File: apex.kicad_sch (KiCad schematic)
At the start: 15 parts, among them J1 USB_C_Receptacle_USB2.0_16P, U1 AP7363-33D-13, U2 USBLC6-2P6

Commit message: re-added symbols
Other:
- note added: "5v-to-3.3v"
- note added: "GND-to-SHIELD"
- note added: "ON LIGHT"
- note added: "USB Configuration Channel"
- note added: "USB ESD Protection"
- note added: "USB-C Connector"
- moved on the sheet: C1, C2, C3, H1, H2, H3, H4, J1, LED1, R1, R2, R3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

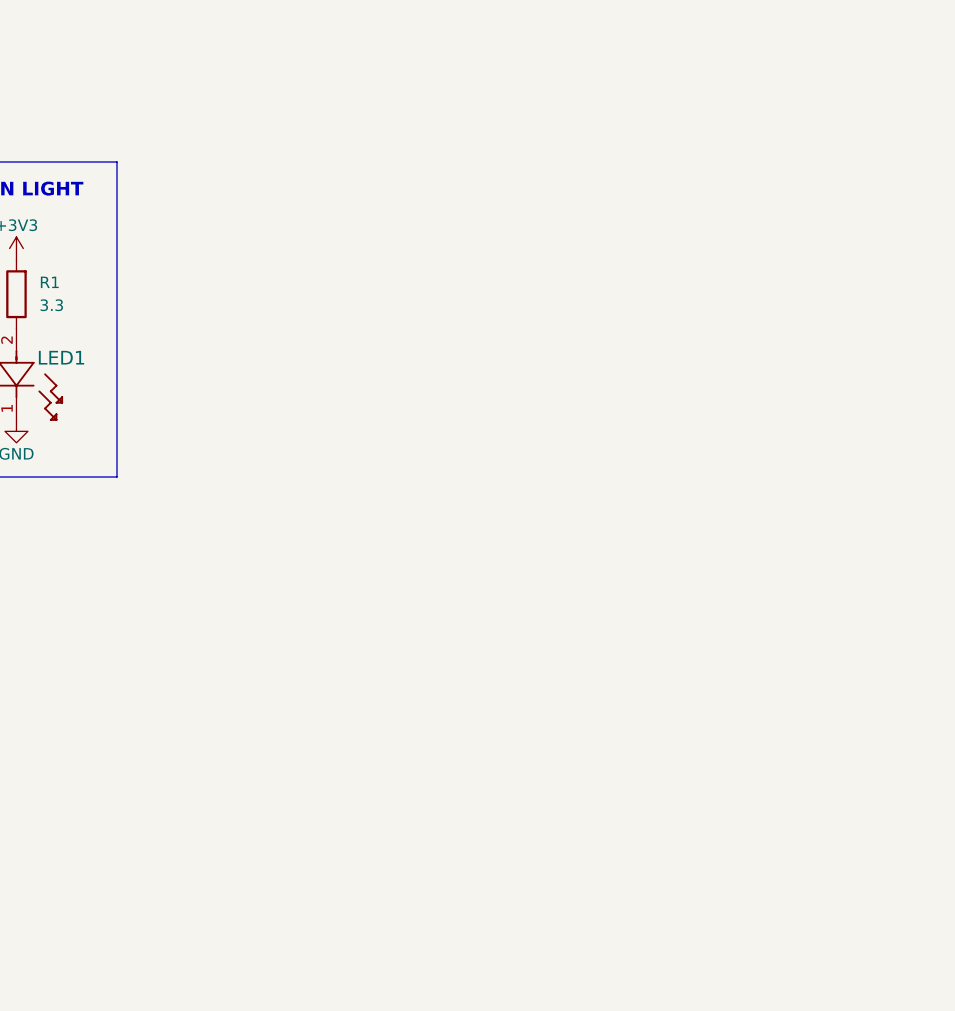
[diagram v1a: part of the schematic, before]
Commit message: started footprint
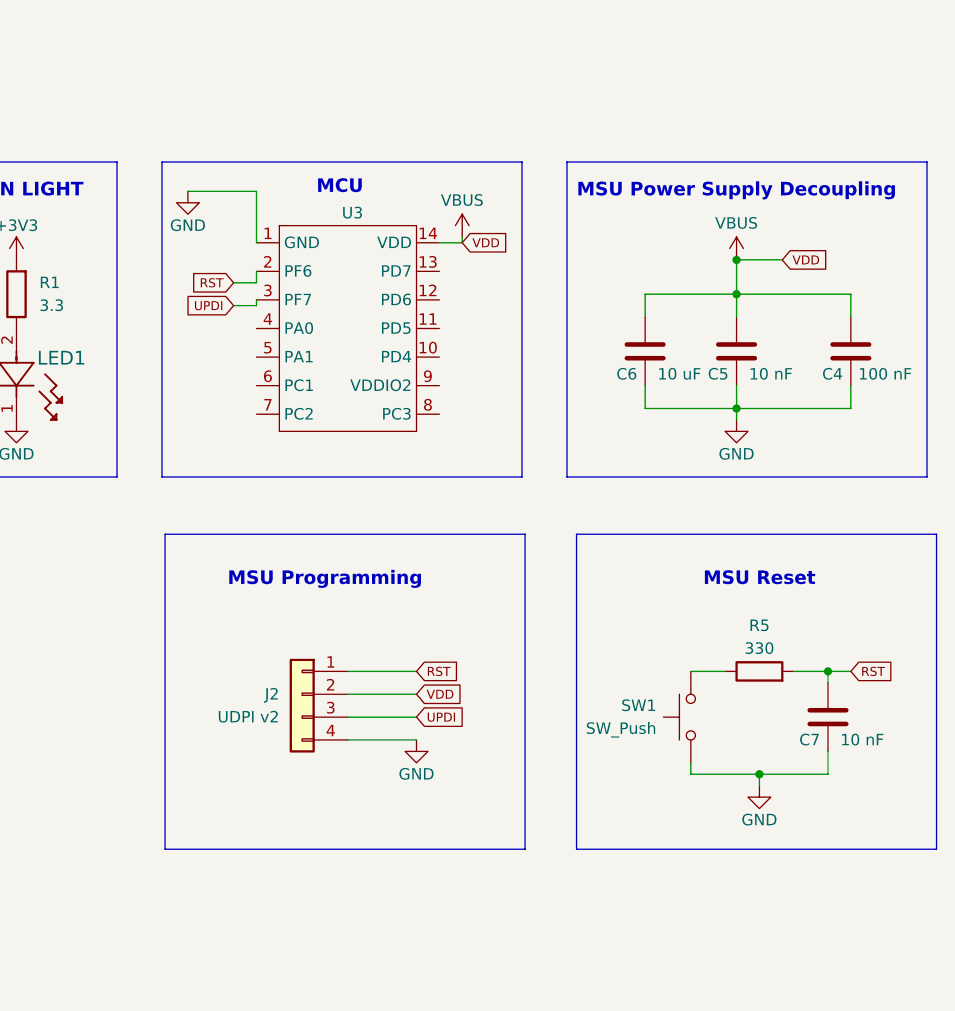
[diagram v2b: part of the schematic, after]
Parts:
- added C4: 100 nF, Capacitor_SMD:C_0805_2012Metric, symbol Device:C
- added C5, C7: 10 nF, Capacitor_SMD:C_0805_2012Metric, symbol Device:C
- added C6: 10 uF, Capacitor_SMD:C_0805_2012Metric, symbol Device:C
- added J2: UDPI v2, symbol Connector_Generic:Conn_01x04
- added R5: 330, Resistor_SMD:R_0805_2012Metric, symbol Device:R
- added SW1: SW_Push, symbol Switch:SW_Push
- added U3: ~, symbol avr66dd14:AVR66DD14
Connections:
- net GND: now also C4.1, C5.1, C6.1, C7.1, J2.4 (Pin_4), SW1.2, U3.1 (GND)
- net VBUS: now also C4.2, C5.2, C6.2, J2.2 (Pin_2), U3.14 (VDD)
- new net: R5.1, SW1.1
- new net RST: C7.2, J2.1 (Pin_1), R5.2, U3.2 (PF6)
- new net UPDI: J2.3 (Pin_3), U3.3 (PF7)
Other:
- note added: "MCU"
- note added: "MSU Power Supply Decoupling"
- note added: "MSU Programming"
- note added: "MSU Reset"

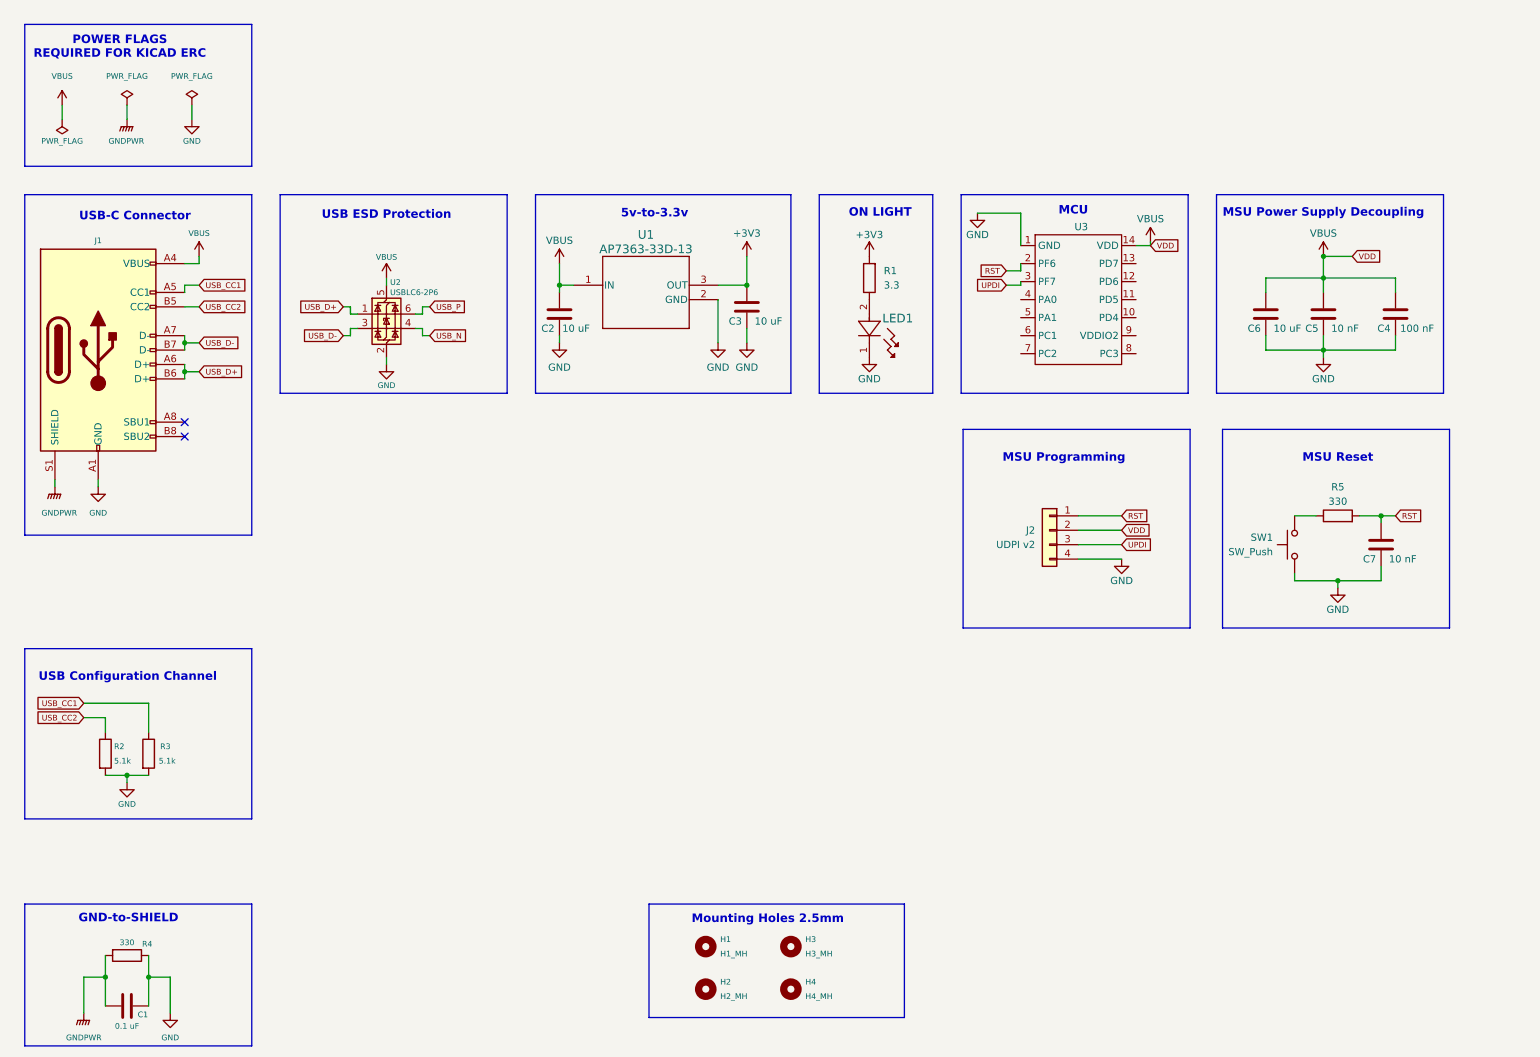
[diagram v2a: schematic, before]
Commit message: added split worksheets
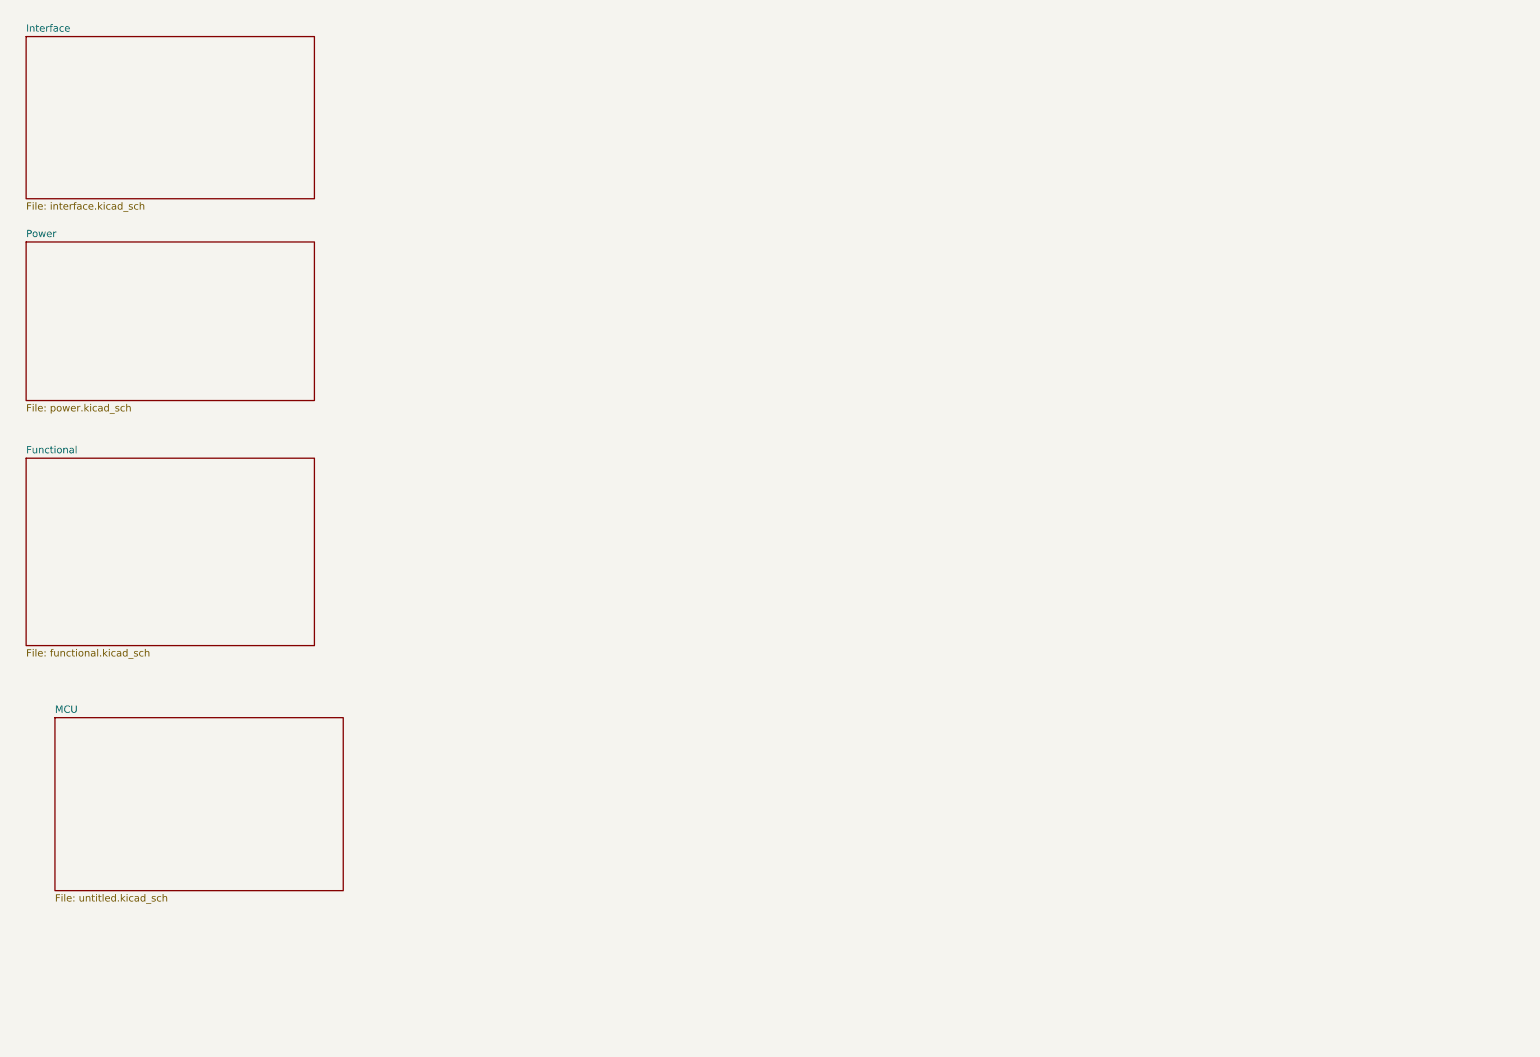
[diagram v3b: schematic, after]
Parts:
- removed C1: 0.1 uF, Capacitor_SMD:C_0805_2012Metric, symbol Device:C
- removed C2, C3, C6: 10 uF, Capacitor_SMD:C_0805_2012Metric, symbol Device:C
- removed C4: 100 nF, Capacitor_SMD:C_0805_2012Metric, symbol Device:C
- removed C5, C7: 10 nF, Capacitor_SMD:C_0805_2012Metric, symbol Device:C
- removed H1: H1_MH, MountingHole:MountingHole_2.5mm_Pad, symbol Mechanical:MountingHole
- removed H2: H2_MH, MountingHole:MountingHole_2.5mm_Pad, symbol Mechanical:MountingHole
- removed H3: H3_MH, MountingHole:MountingHole_2.5mm_Pad, symbol Mechanical:MountingHole
- removed H4: H4_MH, MountingHole:MountingHole_2.5mm_Pad, symbol Mechanical:MountingHole
- removed J1: USB_C_Receptacle_USB2.0_16P, Connector_USB:USB_C_Receptacle_GCT_USB4110, symbol Connector:USB_C_Receptacle_USB2.0_16P
- removed J2: UDPI v2, symbol Connector_Generic:Conn_01x04
- removed LED1: 150080BS75000, LEDBS75000_WRE:LED_BS75000_WRE, symbol 150080BS75000:150080BS75000
- removed R1: 3.3, Resistor_SMD:R_0805_2012Metric, symbol Device:R
- removed R2, R3: 5.1k, Resistor_SMD:R_0805_2012Metric, symbol Device:R
- removed R4, R5: 330, Resistor_SMD:R_0805_2012Metric, symbol Device:R
- removed SW1: SW_Push, symbol Switch:SW_Push
- removed U1: AP7363-33D-13, AP7363_33D_13:TO252-3L_DIO, symbol AP7363_33D_13:AP7363-33D-13
- removed U2: USBLC6-2P6, Package_TO_SOT_SMD:SOT-666, symbol Power_Protection:USBLC6-2P6
- removed U3: ~, symbol avr66dd14:AVR66DD14
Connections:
- no-connect marks 2 -> 0
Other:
- added sheet Functional (functional.kicad_sch)
- added sheet Interface (interface.kicad_sch)
- added sheet MCU (untitled.kicad_sch)
- added sheet Power (power.kicad_sch)
- note removed: "5v-to-3.3v"
- note removed: "GND-to-SHIELD"
- note removed: "MCU"
- note removed: "MSU Power Supply Decoupling"
- note removed: "MSU Programming"
- note removed: "MSU Reset"
- note removed: "Mounting Holes 2.5mm"
- note removed: "ON LIGHT"
- note removed: "POWER FLAGS REQUIRED FOR KICAD ERC"
- note removed: "USB Configuration Channel"
- note removed: "USB ESD Protection"
- note removed: "USB-C Connector"

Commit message: finished ERC, matched footprints, populated 3D models
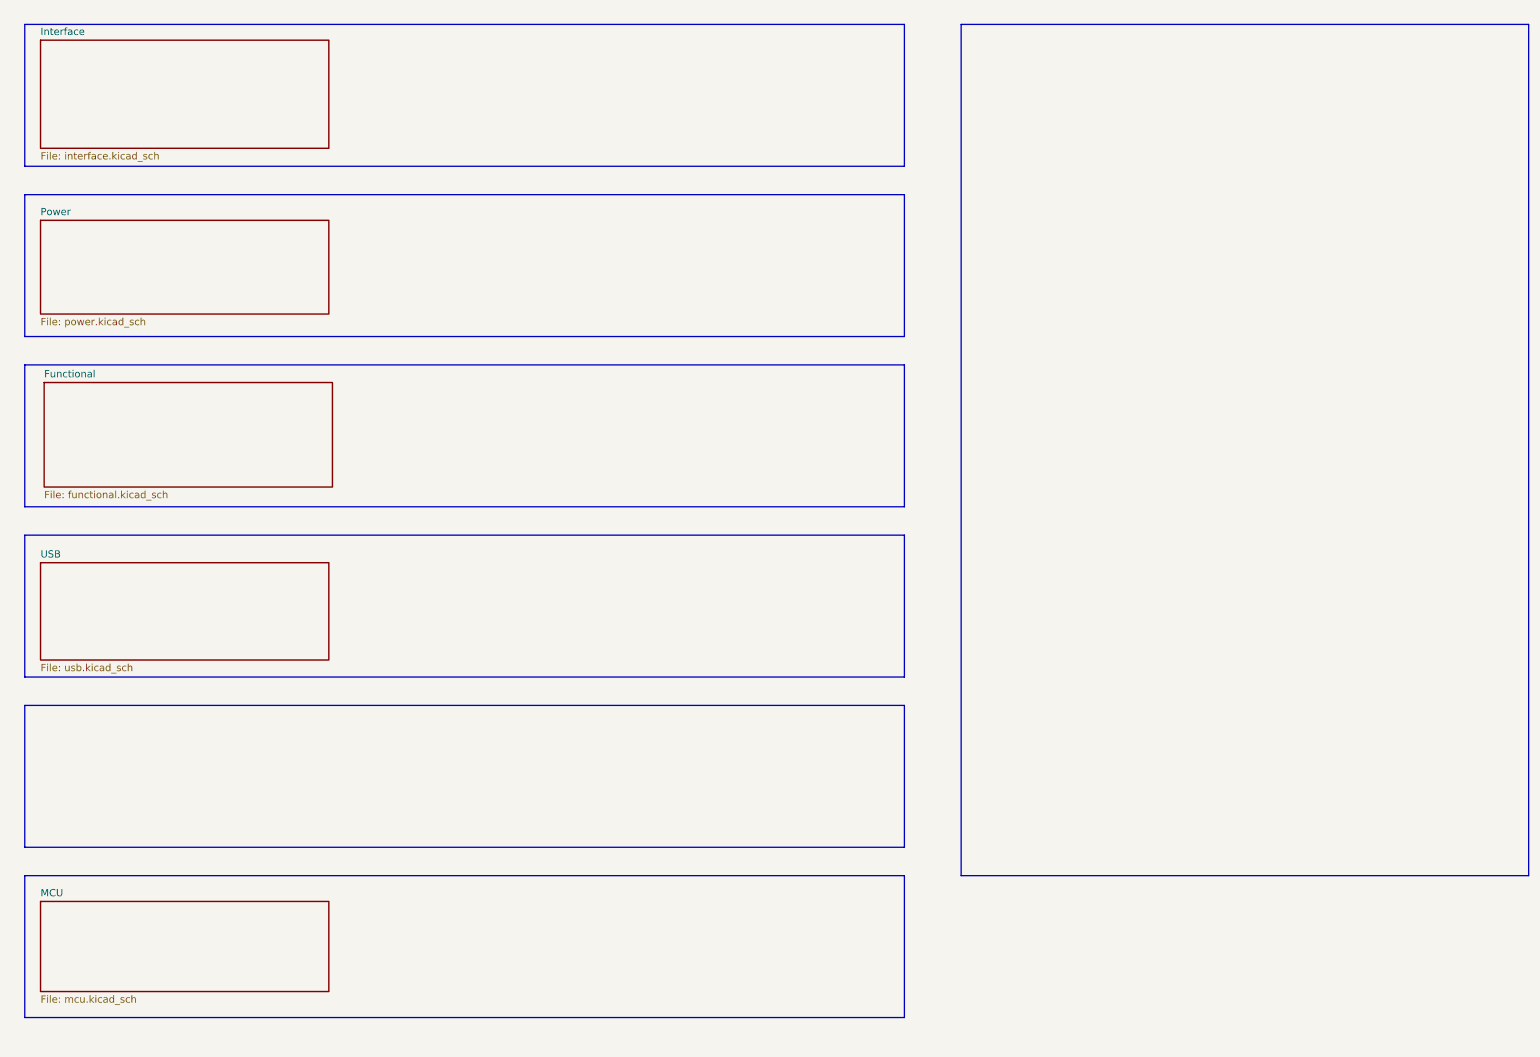
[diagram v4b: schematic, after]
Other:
- added sheet USB (usb.kicad_sch)
- sheet MCU: file untitled.kicad_sch -> mcu.kicad_sch
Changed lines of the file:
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@@
 		(company "InFlynn Technologies")
 	)
-	(sheet
-		(at 20.32 137.16)
-		(size 50.8 30.48)
-		(fields_autoplaced yes)
-		(stroke
-			(width 0.1524)
+	(rectangle
+		(start 15 165)
+		(end 170 190)
+		(stroke
+			(width 0)
+			(type default)
+		)
+		(fill
+			(type none)
+		)
+	)
+	(rectangle
+		(start 15 75)
+		(end 170 100)
+		(stroke
+			(width 0)
+			(type default)
+		)
+		(fill
+			(type none)
+		)
+	)
+	(rectangle
+		(start 15 15)
+		(end 170 40)
+		(stroke
+			(width 0)
+			(type default)
+		)
+		(fill
+			(type none)
+		)
+	)
+	(rectangle
+		(start 15 45)
+		(end 170 70)
+		(stroke
+			(width 0)
+			(type default)
+		)
+		(fill
+			(type none)
+		)
+	)
+	(rectangle
+		(start 15 105)
+		(end 170 130)
+		(stroke
+			(width 0)
+			(type default)
+		)
+		(fill
+			(type none)
+		)
+	)
+	(rectangle
+		(start 15 135)
+		(end 170 160)
+		(stroke
+			(width 0)
+			(type default)
+		)
+		(fill
+			(type none)
+		)
+	)
+	(rectangle
+		(start 180 15)
+		(end 280 165)
+		(stroke
+			(width 0)
+			(type default)
+		)
+		(fill
+			(type none)
+		)
+	)
+	(sheet
+		(at 17.78 169.545)
+		(size 50.8 15.875)
+		(fields_autoplaced yes)
+		(stroke
+			(width 0.25)
 			(type solid)
 		)
@@
 		)
 		(property "Sheetname" "MCU"
-			(at 20.32 136.4484 0)
-			(effects
-				(font
-					(size 1.27 1.27)
-				)
-				(justify left bottom)
-			)
-		)
-		(property "Sheetfile" "untitled.kicad_sch"
-			(at 20.32 168.2246 0)
+			(at 17.78 168.7846 0)
+			(effects
+				(font
+					(size 1.27 1.27)
+				)
+				(justify left bottom)
+			)
+		)
+		(property "Sheetfile" "mcu.kicad_sch"
+			(at 17.78 186.0534 0)
 			(effects
 				(font
@@
 	)
 	(sheet
-		(at 15.24 91.44)
-		(size 50.8 33.02)
-		(fields_autoplaced yes)
-		(stroke
-			(width 0.1524)
+		(at 17.78 109.855)
+		(size 50.8 17.145)
+		(fields_autoplaced yes)
+		(stroke
+			(width 0.25)
+			(type solid)
+		)
+		(fill
+			(color 0 0 0 0.0000)
+		)
+		(property "Sheetname" "USB"
+			(at 17.78 109.0946 0)
+			(effects
+				(font
+					(size 1.27 1.27)
+				)
+				(justify left bottom)
+			)
+		)
+		(property "Sheetfile" "usb.kicad_sch"
+			(at 17.78 127.6334 0)
+			(effects
+				(font
+					(size 1.27 1.27)
+				)
+				(justify left top)
+			)
+		)
+		(instances
+			(project "apex"
+				(path "/84b8b555-aaa5-476b-b0f2-2d0f894bf0e6"
+					(page "6")
+				)
+			)
+		)
+	)
+	(sheet
+		(at 18.415 78.105)
+		(size 50.8 18.415)
+		(fields_autoplaced yes)
+		(stroke
+			(width 0.25)
 			(type solid)
 		)
@@
 		)
 		(property "Sheetname" "Functional"
-			(at 15.24 90.7284 0)
+			(at 18.415 77.3446 0)
 			(effects
 				(font
@@
 		)
 		(property "Sheetfile" "functional.kicad_sch"
-			(at 15.24 125.0446 0)
+			(at 18.415 97.1534 0)
 			(effects
 				(font
@@
 	)
 	(sheet
-		(at 15.24 53.34)
-		(size 50.8 27.94)
-		(fields_autoplaced yes)
-		(stroke
-			(width 0.1524)
+		(at 17.78 49.53)
+		(size 50.8 16.51)
+		(fields_autoplaced yes)
+		(stroke
+			(width 0.25)
 			(type solid)
 		)
@@
 		)
 		(property "Sheetname" "Power"
-			(at 15.24 52.6284 0)
+			(at 17.78 48.7696 0)
 			(effects
 				(font
@@
 		)
 		(property "Sheetfile" "power.kicad_sch"
-			(at 15.24 81.8646 0)
+			(at 17.78 66.6734 0)
 			(effects
 				(font
@@
 	)
 	(sheet
-		(at 15.24 17.145)
-		(size 50.8 28.575)
-		(fields_autoplaced yes)
-		(stroke
-			(width 0.1524)
+		(at 17.78 17.78)
+		(size 50.8 19.05)
+		(fields_autoplaced yes)
+		(stroke
+			(width 0.25)
 			(type solid)
 		)
@@
 		)
 		(property "Sheetname" "Interface"
-			(at 15.24 16.4334 0)
+			(at 17.78 17.0196 0)
 			(effects
 				(font
@@
 		)
 		(property "Sheetfile" "interface.kicad_sch"
-			(at 15.24 46.3046 0)
-			(effects
-				(font
+			(at 17.78 37.4634 0)
+			(effects
+				(font
